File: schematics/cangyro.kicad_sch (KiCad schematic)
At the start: 14 parts, among them J1 Conn_01x06 CAN & PWR, J2 Conn_01x10 IMU BNO080, P1 USB_C_Plug_USB2.0 Serial, SW1 SW_Push IMU_RST, U1 STM32G474CBTx, U2 MCP2562-E-MF, U3 AP2112K-3.3

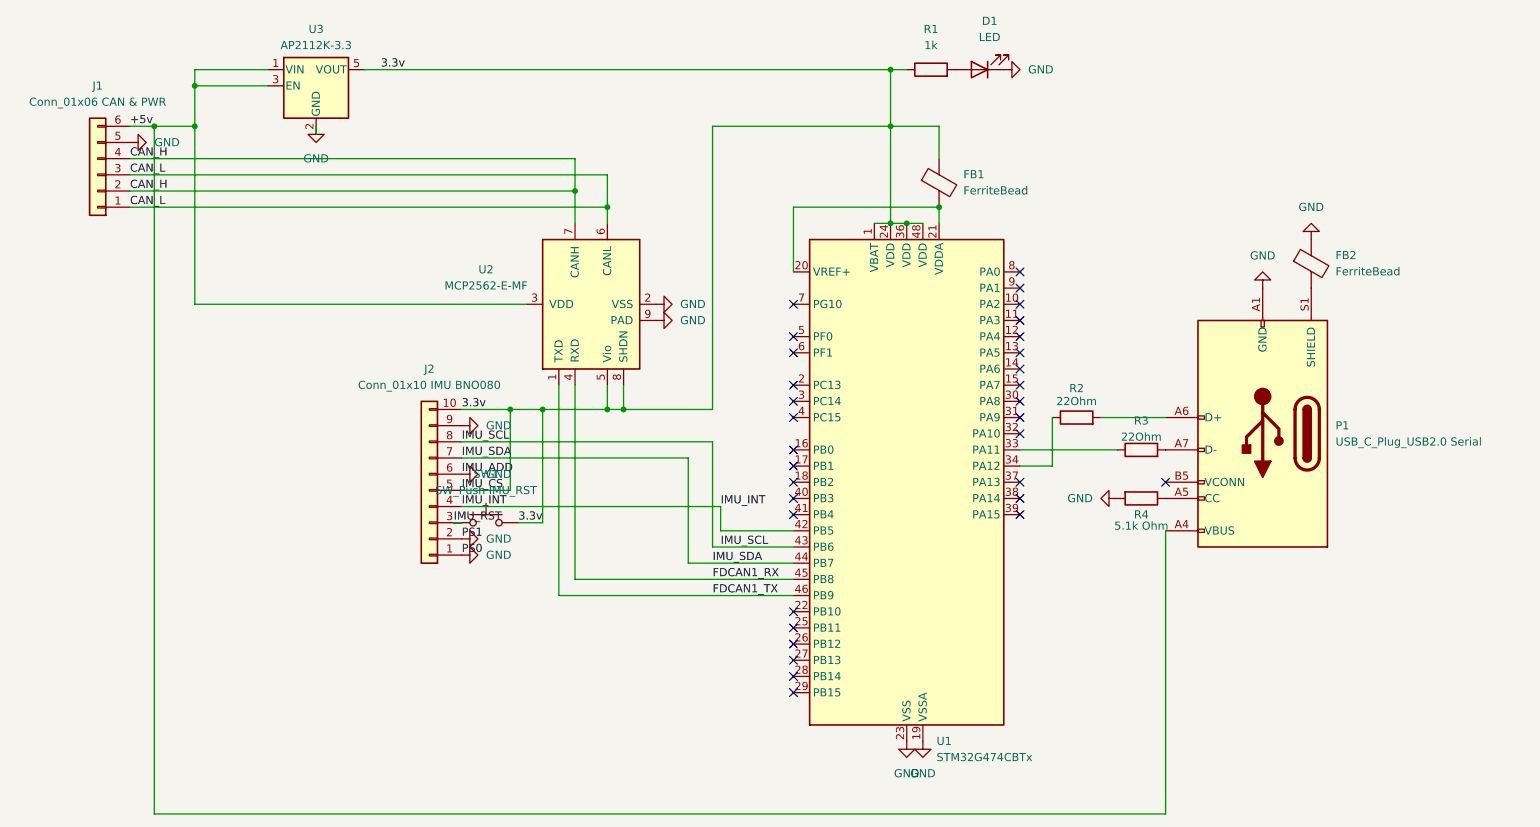
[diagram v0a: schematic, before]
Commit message: Switched MicroController To PiPco
- Base software with BNO08x lib and pico stuff
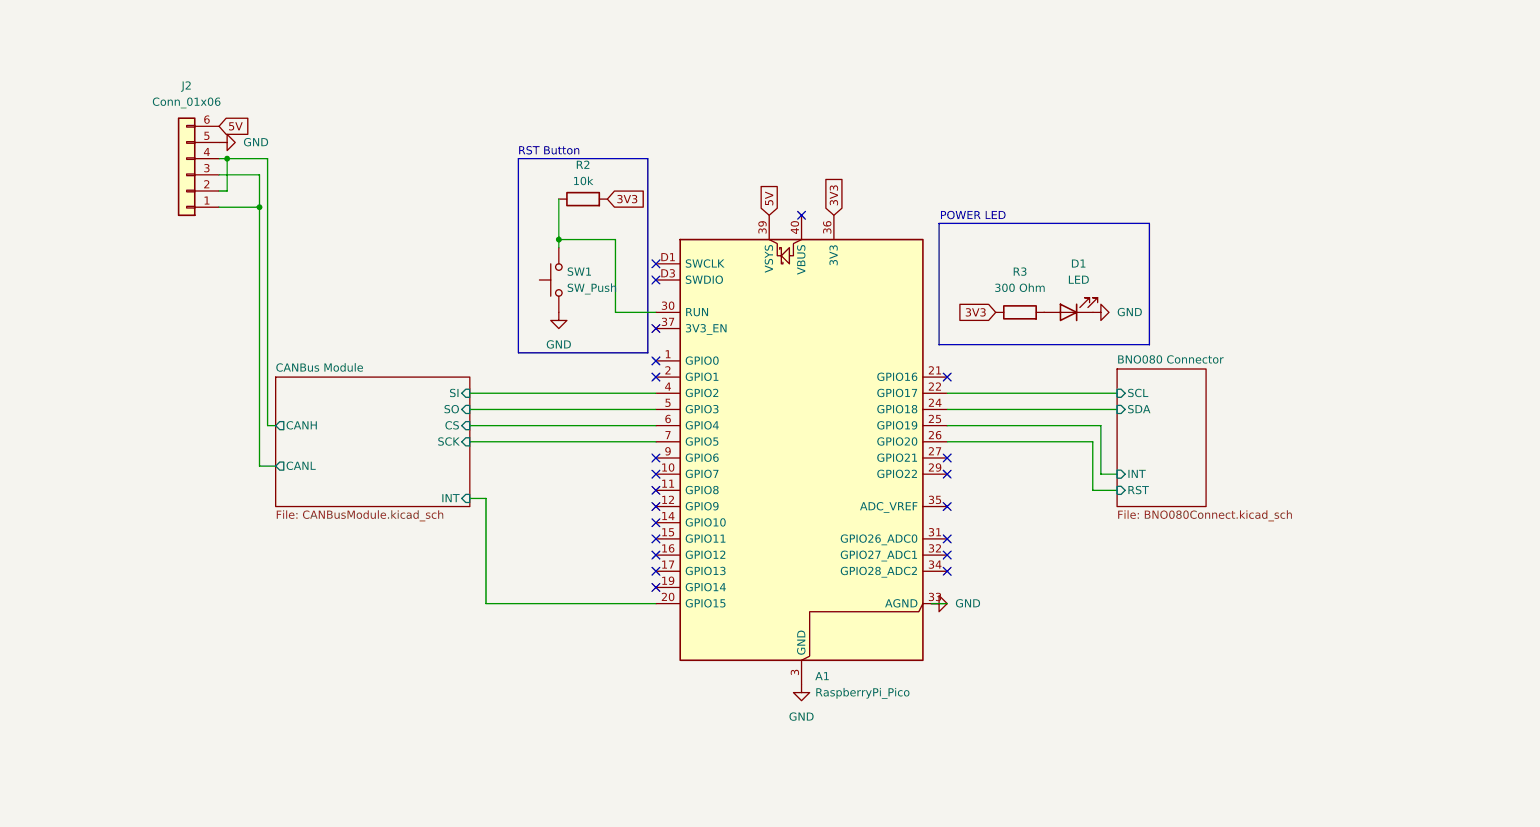
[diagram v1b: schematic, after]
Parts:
- removed FB1, FB2: FerriteBead, Inductor_SMD:L_0805_2012Metric, symbol Device:FerriteBead
- removed J1: Conn_01x06 CAN & PWR, TerminalBlock_Phoenix:TerminalBlock_Phoenix_MKDS-1,5-6-5.08_1x06_P5.08mm_Horizontal, symbol Connector_Generic:Conn_01x06
- removed J2: Conn_01x10 IMU BNO080, Connector_PinSocket_1.00mm:PinSocket_1x10_P1.00mm_Vertical, symbol Connector_Generic:Conn_01x10
- removed P1: USB_C_Plug_USB2.0 Serial, Connector_USB:USB_C_Receptacle_HRO_TYPE-C-31-M-17, symbol Connector:USB_C_Plug_USB2.0
- removed R1: 1k, Resistor_SMD:R_0805_2012Metric, symbol Device:R
- removed R4: 5.1k Ohm, Resistor_SMD:R_0805_2012Metric, symbol Device:R
- removed U1: STM32G474CBTx, Package_QFP:LQFP-48_7x7mm_P0.5mm, symbol MCU_ST_STM32G4:STM32G474CBTx
- removed U2: MCP2562-E-MF, Package_DFN_QFN:DFN-8-1EP_3x3mm_P0.65mm_EP1.55x2.4mm, symbol Interface_CAN_LIN:MCP2562-E-MF
- removed U3: AP2112K-3.3, Package_TO_SOT_SMD:SOT-23-5, symbol Regulator_Linear:AP2112K-3.3
- added A1: RaspberryPi_Pico, Module:RaspberryPi_Pico_SMD_HandSolder, symbol MCU_Module:RaspberryPi_Pico_Debug
- added J2: Conn_01x06, symbol Connector_Generic:Conn_01x06
- D1: footprint LED_SMD:LED_0805_2012Metric -> (none)
- R2: value 22Ohm -> 10k; footprint Resistor_SMD:R_0805_2012Metric -> (none)
- R3: value 22Ohm -> 300 Ohm; footprint Resistor_SMD:R_0805_2012Metric -> (none)
- SW1: value SW_Push IMU_RST -> SW_Push; footprint Button_Switch_SMD:SW_SPST_TL3342 -> (none)
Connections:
- net 3.3v is gone; now on an unnamed net: SW1.2
- net IMU_RST is gone; now on net GND: SW1.1
- net GND: now also A1.13 (GND), A1.18 (GND), A1.23 (GND), A1.28 (GND), A1.3 (GND), A1.33 (AGND), A1.38 (GND), A1.8 (GND), A1.D2 (GND), J2.5 (Pin_5)
- net at D1.2 (A): now also R3.2
- net 3V3: now reaches R2.2
- net 3V3: now also R3.1, A1.36 (3V3)
- net at R2.1: now also A1.30 (RUN)
- new net 5V: A1.39 (VSYS), J2.6 (Pin_6)
- new net BNO080 Connector/INT: A1.25 (GPIO19)
- new net BNO080 Connector/RST: A1.26 (GPIO20)
- new net BNO080 Connector/SCL: A1.22 (GPIO17)
- new net BNO080 Connector/SDA: A1.24 (GPIO18)
- new net CANBus Module/CANH: J2.2 (Pin_2), J2.4 (Pin_4)
- new net CANBus Module/CANL: J2.1 (Pin_1), J2.3 (Pin_3)
- new net CANBus Module/CS: A1.6 (GPIO4)
- new net CANBus Module/INT: A1.20 (GPIO15)
- new net CANBus Module/SCK: A1.7 (GPIO5)
- new net CANBus Module/SI: A1.4 (GPIO2)
- new net CANBus Module/SO: A1.5 (GPIO3)
- no-connect marks 32 -> 22
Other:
- added sheet BNO080 Connector (BNO080Connect.kicad_sch)
- added sheet CANBus Module (CANBusModule.kicad_sch)
- note added: "POWER LED"
- note added: "RST Button"

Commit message: Added Footprints
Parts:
- D1: footprint (none) -> LED_SMD:LED_0603_1608Metric
- J2: footprint (none) -> TerminalBlock_Phoenix:TerminalBlock_Phoenix_MKDS-1,5-6_1x06_P5.00mm_Horizontal
- R2, R3: footprint (none) -> Resistor_SMD:R_0603_1608Metric
- SW1: footprint (none) -> Button_Switch_SMD:SW_Push_1P1T_NO_CK_KMR2
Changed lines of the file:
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@@
 			)
 		)
-		(property "Footprint" ""
+		(property "Footprint" "TerminalBlock_Phoenix:TerminalBlock_Phoenix_MKDS-1,5-6_1x06_P5.00mm_Horizontal"
 			(at 54.61 58.42 0)
 			(effects
@@
 			)
 		)
-		(property "Footprint" ""
+		(property "Footprint" "Resistor_SMD:R_0603_1608Metric"
 			(at 116.84 64.008 90)
 			(effects
@@
 			)
 		)
-		(property "Footprint" ""
+		(property "Footprint" "Button_Switch_SMD:SW_Push_1P1T_NO_CK_KMR2"
 			(at 107.95 74.93 0)
 			(effects
@@
 			)
 		)
-		(property "Footprint" ""
+		(property "Footprint" "Resistor_SMD:R_0603_1608Metric"
 			(at 185.42 81.788 90)
 			(effects
@@
 			)
 		)
-		(property "Footprint" ""
+		(property "Footprint" "LED_SMD:LED_0603_1608Metric"
 			(at 193.04 80.01 0)
 			(effects
